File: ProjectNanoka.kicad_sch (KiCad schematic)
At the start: 32 parts, among them K1 2-1462038-1, P1 ST_20A, Q1 2N3904BU, Q2 2N3904BU, U1 TLV70033DDCR, U2 NC7WZ16P6X, U3 PS1440P02BT

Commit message: Clean up the board from old components
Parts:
- removed C2: 47uF, Footprints:CAP_UUQ_5X5P4_NCH, symbol Symbols:C
- removed C3, C5: 100nF, Footprints:CAP_C320_KEM, symbol Symbols:C
- removed D1: 1N4148, Footprints:D_DO-35_SOD27_P7.62mm_Horizontal, symbol Symbols:1N4148
- removed K1: 2-1462038-1, Footprints:RELAY8-TH_NON-LATCH_1-COIL, symbol Symbols:2-1462038-1
- removed Q1: 2N3904BU, Footprints:2N3904BU, symbol Symbols:2N3904BU
- removed R1: 1.8k, Footprints:STA_CF14_STP, symbol Symbols:R
- removed R2: 100, Footprints:STA_CF14_STP, symbol Symbols:R
- removed R3: 10k, Footprints:STA_RNF14_STP, symbol Symbols:R
- removed R4: 1k, Footprints:STA_RNF14_STP, symbol Symbols:R
- removed R8: 220, Footprints:STA_RNMF14_STP, symbol Symbols:R
- removed U2: NC7WZ16P6X, Footprints:SOT65P210X110-6N, symbol Symbols:NC7WZ16P6X
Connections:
- net GNDPWR: now also GT1.2 (Pin_2); no longer A_OUT1.1 (Pin_1), GT1.1 (Pin_1)
- net at A1.2 (GPIO1): no longer GT1.2 (Pin_2)
- net at A1.11 (GPIO8): no longer GT3.2 (Pin_2)
- net at A1.14 (GPIO10): no longer GT4.1 (Pin_1)
- net at A1.16 (GPIO12): no longer GT4.2 (Pin_2)
- net at A1.5 (GPIO3): no longer GT2.1 (Pin_1)
- net at A1.7 (GPIO5): no longer GT2.2 (Pin_2)
- net at A1.9 (GPIO6): no longer GT3.1 (Pin_1)
- net AIN: no longer names the net of A_IN1.2 (Pin_2)
- net AOUT: no longer names the net of A_OUT1.2 (Pin_2)
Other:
- moved on the sheet: GT1, GT2, GT3, GT4, R6

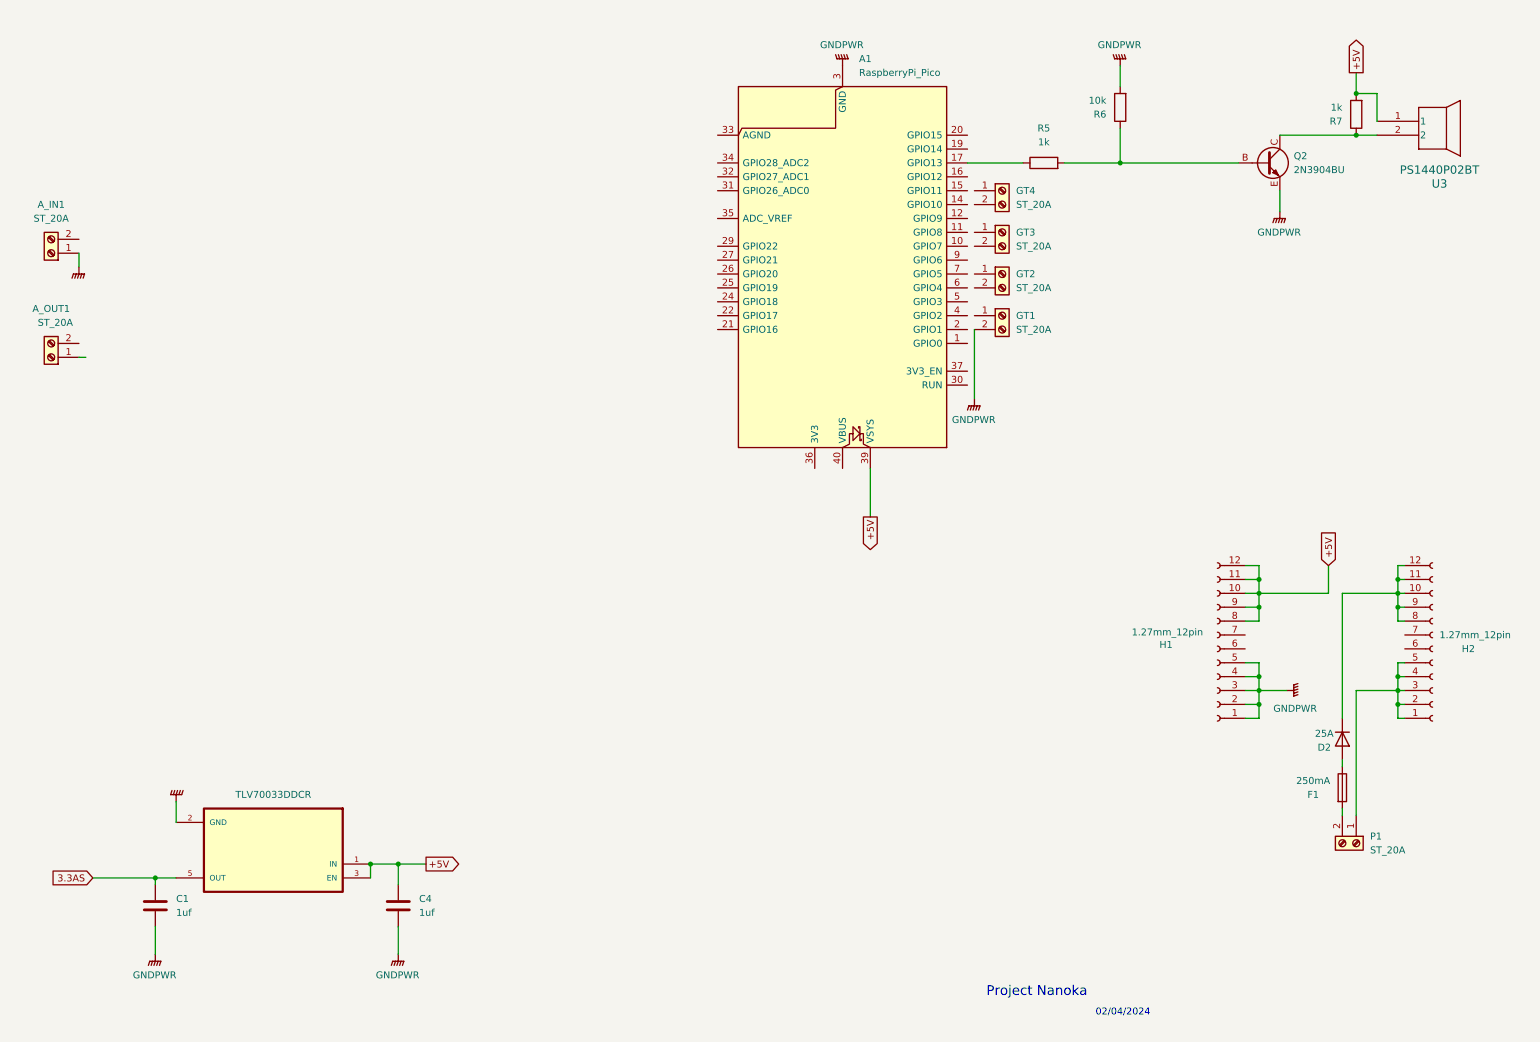
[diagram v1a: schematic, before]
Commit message: Update board with new layout and schematic
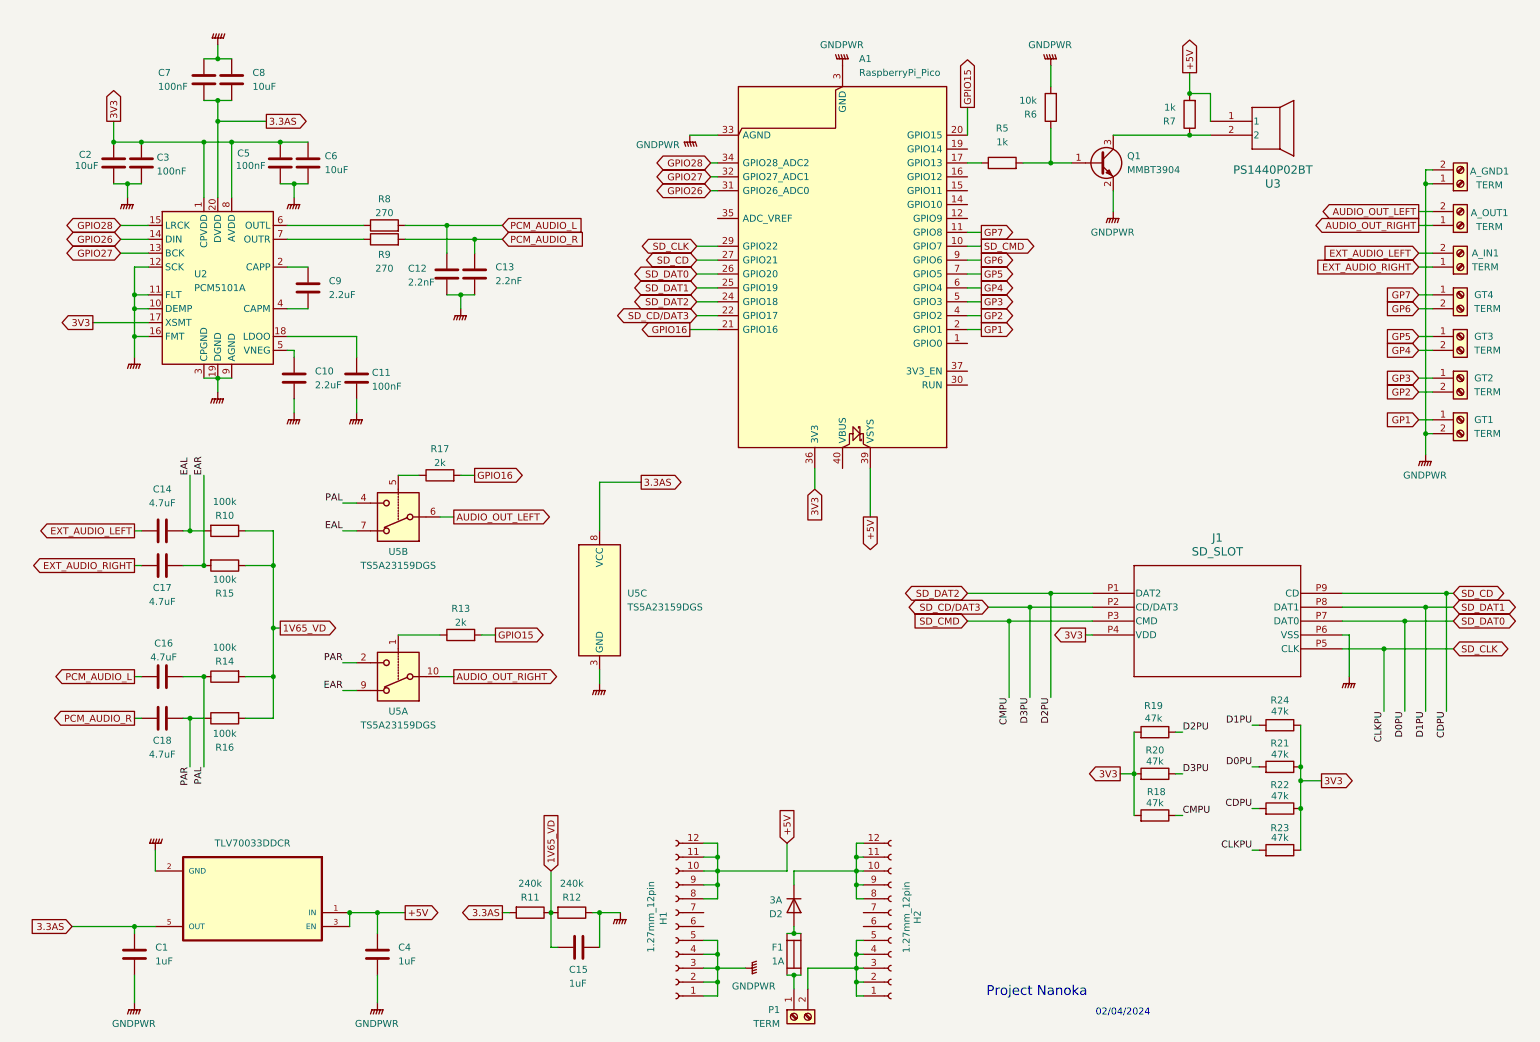
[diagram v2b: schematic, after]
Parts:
- removed Q2: 2N3904BU, Footprints:2N3904BU, symbol Symbols:2N3904BU
- added A_GND1: TERM, NewFootprints:TERMINAL, symbol Symbols:Screw_Terminal_01x02
- added C10, C9: 2.2uF, Capacitor_SMD:C_0402_1005Metric, symbol Device:C
- added C11, C3, C5, C7: 100nF, Capacitor_SMD:C_0402_1005Metric, symbol Device:C
- added C12, C13: 2.2nF, Capacitor_SMD:C_0402_1005Metric, symbol Device:C
- added C14, C16, C17, C18: 4.7uF, Capacitor_SMD:C_0402_1005Metric, symbol Device:C
- added C15: 1uF, Capacitor_SMD:C_0402_1005Metric, symbol Device:C
- added C2, C6, C8: 10uF, Capacitor_SMD:C_0402_1005Metric, symbol Device:C
- added J1: SD_SLOT, NewFootprints:SD_SLOT, symbol Symbols:SD_SLOT
- added Q1: MMBT3904, Package_TO_SOT_SMD:SOT-23, symbol Transistor_BJT:MMBT3904
- added R10, R14, R15, R16: 100k, Resistor_SMD:R_0402_1005Metric, symbol Symbols:R
- added R11, R12: 240k, Resistor_SMD:R_0402_1005Metric, symbol Symbols:R
- added R13, R17: 2k, Resistor_SMD:R_0402_1005Metric, symbol Symbols:R
- added R18, R19, R20, R21, R22, R23, R24: 47k, Resistor_SMD:R_0402_1005Metric, symbol Symbols:R
- added R8, R9: 270, Resistor_SMD:R_0402_1005Metric, symbol Symbols:R
- added U2: PCM5101A, Package_SO:TSSOP-20_4.4x6.5mm_P0.65mm, symbol Audio:PCM5101A
- added U5: TS5A23159DGS, Package_SO:TSSOP-10_3x3mm_P0.5mm, symbol Analog_Switch:TS5A23159DGS
- A_IN1, A_OUT1, GT1, GT2, GT3, GT4, P1: value ST_20A -> TERM; footprint Footprints:CONN_1935161_PXC -> NewFootprints:TERMINAL
- C1, C4: value 1uf -> 1uF; footprint Footprints:CAP_C330C_MR_X7R_KEM -> Capacitor_SMD:C_0603_1608Metric
- D2: value 25A -> 3A
- F1: value 250mA -> 1A; footprint Footprints:20x300_FUSE_HOLDER_0PTF0078P_LTF -> NewFootprints:FUSE_HOLDER
- R5, R6, R7: footprint Footprints:STA_RNF14_STP -> Resistor_SMD:R_0603_1608Metric
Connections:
- net 3.3AS: now also C7.2, C8.2, R11.2, U2.20 (DVDD), U5.8 (VCC)
- net GNDPWR: now also A1.33 (AGND), A_GND1.1 (Pin_1), A_GND1.2 (Pin_2), C10.2, C11.2, C12.2, C13.2, C15.2, C2.2, C3.2, C5.2, C6.2, C7.1, C8.1, J1.P6 (VSS), Q1.2 (E), R12.1, U2.10 (DEMP), U2.11 (FLT), U2.12 (SCK), U2.16 (FMT), U2.19 (DGND), U2.3 (CPGND), U2.9 (AGND), U5.3 (GND); no longer A_IN1.1 (Pin_1)
- net AUDIO_OUT_RIGHT: now reaches A_OUT1.1 (Pin_1)
- net AUDIO_OUT_RIGHT: now also U5.10
- net AUDIO_OUT_LEFT: now reaches A_OUT1.2 (Pin_2)
- net AUDIO_OUT_LEFT: now also U5.6
- net at R5.2, R6.1: now also Q1.1 (B)
- net at R7.1, U3.2: now also Q1.3 (C)
- net GP1: now reaches GT1.1 (Pin_1)
- net GP1: now also A1.2 (GPIO1)
- net at H2.1 (Pin_1), H2.2 (Pin_2), H2.3 (Pin_3)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: now also P1.2 (Pin_2); no longer P1.1 (Pin_1)
- net at F1.2: now also F1.1, P1.1 (Pin_1); no longer P1.2 (Pin_2)
- net at D2.2 (A): now also F1.3, F1.4; no longer F1.1
- net SD_CMD: now reaches A1.10 (GPIO7)
- net SD_CMD: now also J1.P3 (CMD), R18.1
- net GP7: now reaches A1.11 (GPIO8)
- net GP7: now also GT4.1 (Pin_1)
- net GPIO15: now reaches A1.20 (GPIO15)
- net GPIO15: now also R13.2
- net GPIO16: now reaches A1.21 (GPIO16)
- net GPIO16: now also R17.2
- net SD_CD/DAT3: now reaches A1.22 (GPIO17)
- net SD_CD/DAT3: now also J1.P2 (CD/DAT3), R20.1
- net SD_DAT2: now reaches A1.24 (GPIO18)
- net SD_DAT2: now also J1.P1 (DAT2), R19.1
- net SD_DAT1: now reaches A1.25 (GPIO19)
- net SD_DAT1: now also J1.P8 (DAT1), R24.2
- net SD_DAT0: now reaches A1.26 (GPIO20)
- net SD_DAT0: now also J1.P7 (DAT0), R21.2
- net SD_CD: now reaches A1.27 (GPIO21)
- net SD_CD: now also J1.P9 (CD), R22.2
- net SD_CLK: now reaches A1.29 (GPIO22)
- net SD_CLK: now also J1.P5 (CLK), R23.2
- net GPIO26: now reaches A1.31 (GPIO26_ADC0)
- net GPIO26: now also U2.14 (DIN)
- net GPIO27: now reaches A1.32 (GPIO27_ADC1)
- net GPIO27: now also U2.13 (BCK)
- net GPIO28: now reaches A1.34 (GPIO28_ADC2)
- net GPIO28: now also U2.15 (LRCK)
- net 3V3: now reaches A1.36 (3V3)
- net 3V3: now also C2.1, C3.1, C5.1, C6.1, J1.P4 (VDD), R18.2, R19.2, R20.2, R21.1, R22.1, R23.1, R24.1, U2.1 (CPVDD), U2.17 (XSMT), U2.8 (AVDD)
- net GP2: now reaches A1.4 (GPIO2)
- net GP2: now also GT2.2 (Pin_2)
- net GP3: now reaches A1.5 (GPIO3)
- net GP3: now also GT2.1 (Pin_1)
- net GP4: now reaches A1.6 (GPIO4)
- net GP4: now also GT3.2 (Pin_2)
- net GP5: now reaches A1.7 (GPIO5)
- net GP5: now also GT3.1 (Pin_1)
- net GP6: now reaches A1.9 (GPIO6)
- net GP6: now also GT4.2 (Pin_2)
- net EXT_AUDIO_LEFT: now reaches A_IN1.2 (Pin_2)
- net EXT_AUDIO_LEFT: now also C14.1
- new net: R9.1, U2.7 (OUTR)
- new net: R13.1, U5.1
- new net: C10.1, U2.5 (VNEG)
- new net: R17.1, U5.5
- new net: C11.1, U2.18 (LDOO)
- new net: C9.1, U2.2 (CAPP)
- new net: C9.2, U2.4 (CAPM)
- new net: R8.1, U2.6 (OUTL)
- new net 1V65_VD: C15.1, R10.1, R11.1, R12.2, R14.2, R15.1, R16.2
- new net EAL: C14.2, R10.2, U5.7
- new net EAR: C17.2, R15.2, U5.9
- new net EXT_AUDIO_RIGHT: A_IN1.1 (Pin_1), C17.1
- new net PAL: C16.1, R14.1, U5.4
- new net PAR: C18.1, R16.1, U5.2
- new net PCM_AUDIO_L: C12.1, C16.2, R8.2
- new net PCM_AUDIO_R: C13.1, C18.2, R9.2
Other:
- moved on the sheet: C1, C4, D2, GT1, GT2, GT3, GT4, H1, H2, P1, R5, R6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
